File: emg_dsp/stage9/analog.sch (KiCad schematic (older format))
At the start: 27 parts, among them U35 OMNETICS_36, U36 MIC5365-2.7, U37 TC1016-3.0, U39 9X100, U40 ADCS7476, U41 9X100, U45 RHA2132

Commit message: boards done!! now need to produce gerbers etc.
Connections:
- wire segments 117 -> 113
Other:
- moved on the sheet: R47, R48, R52, R54

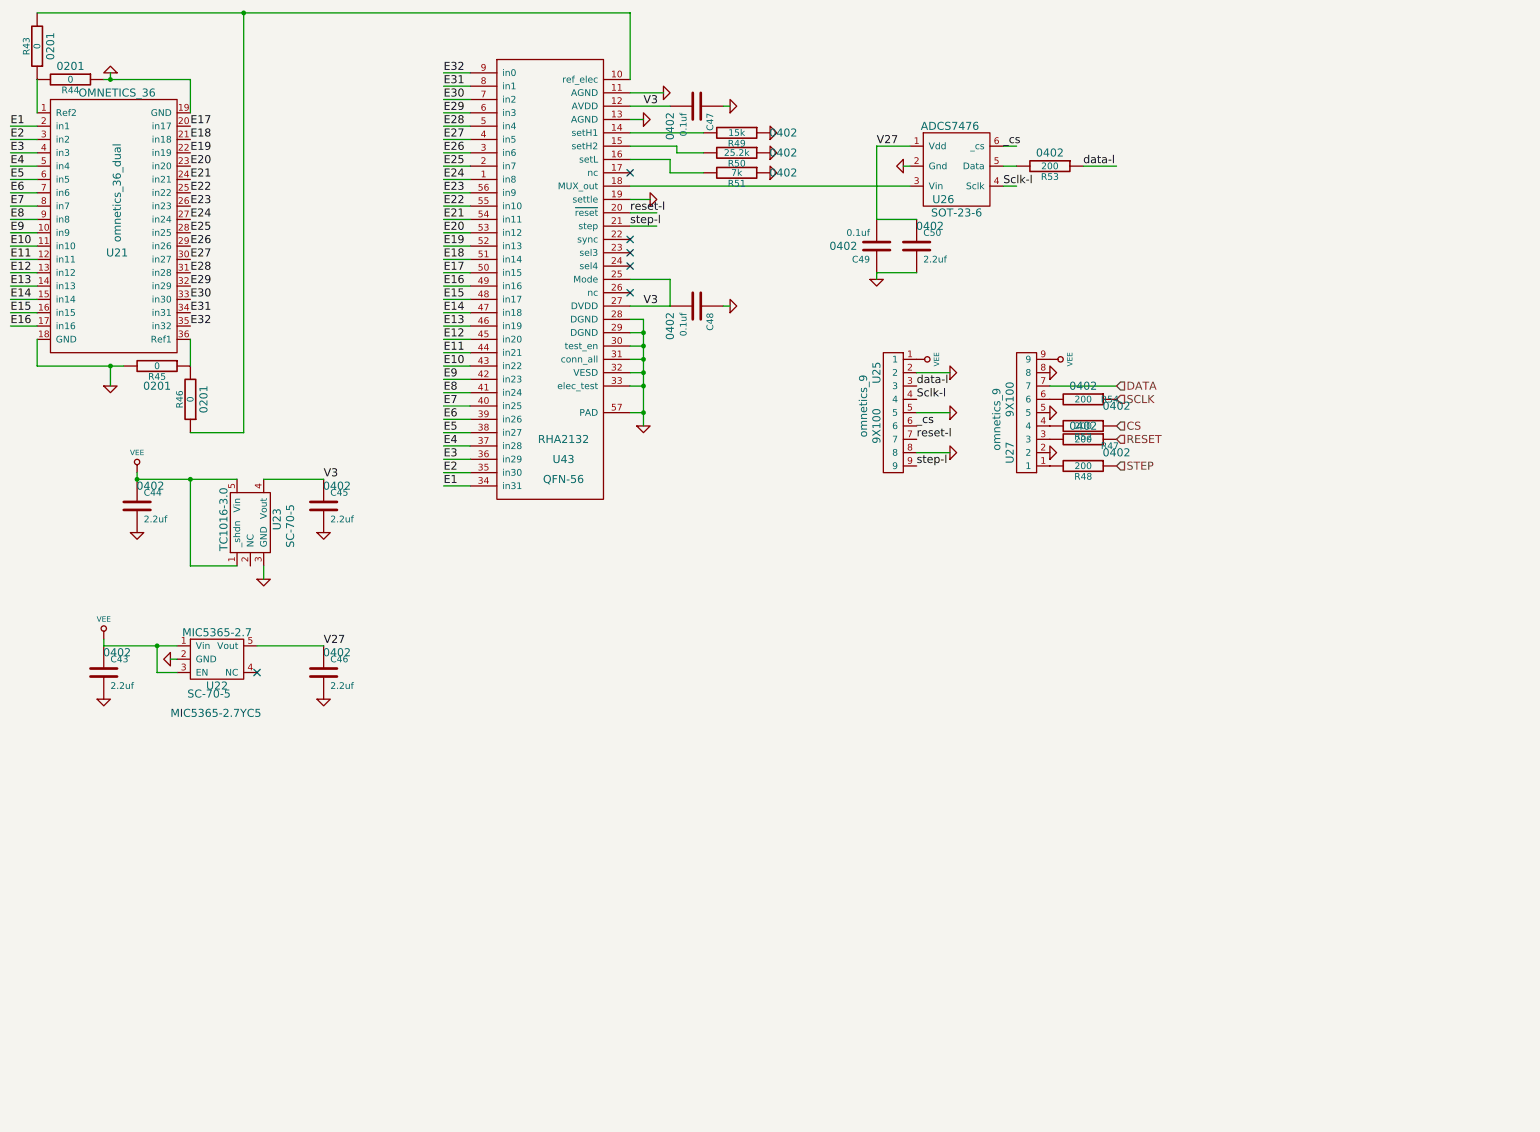
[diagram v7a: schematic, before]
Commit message: cleaned up firingrate.h -- not sure why this was not commited!
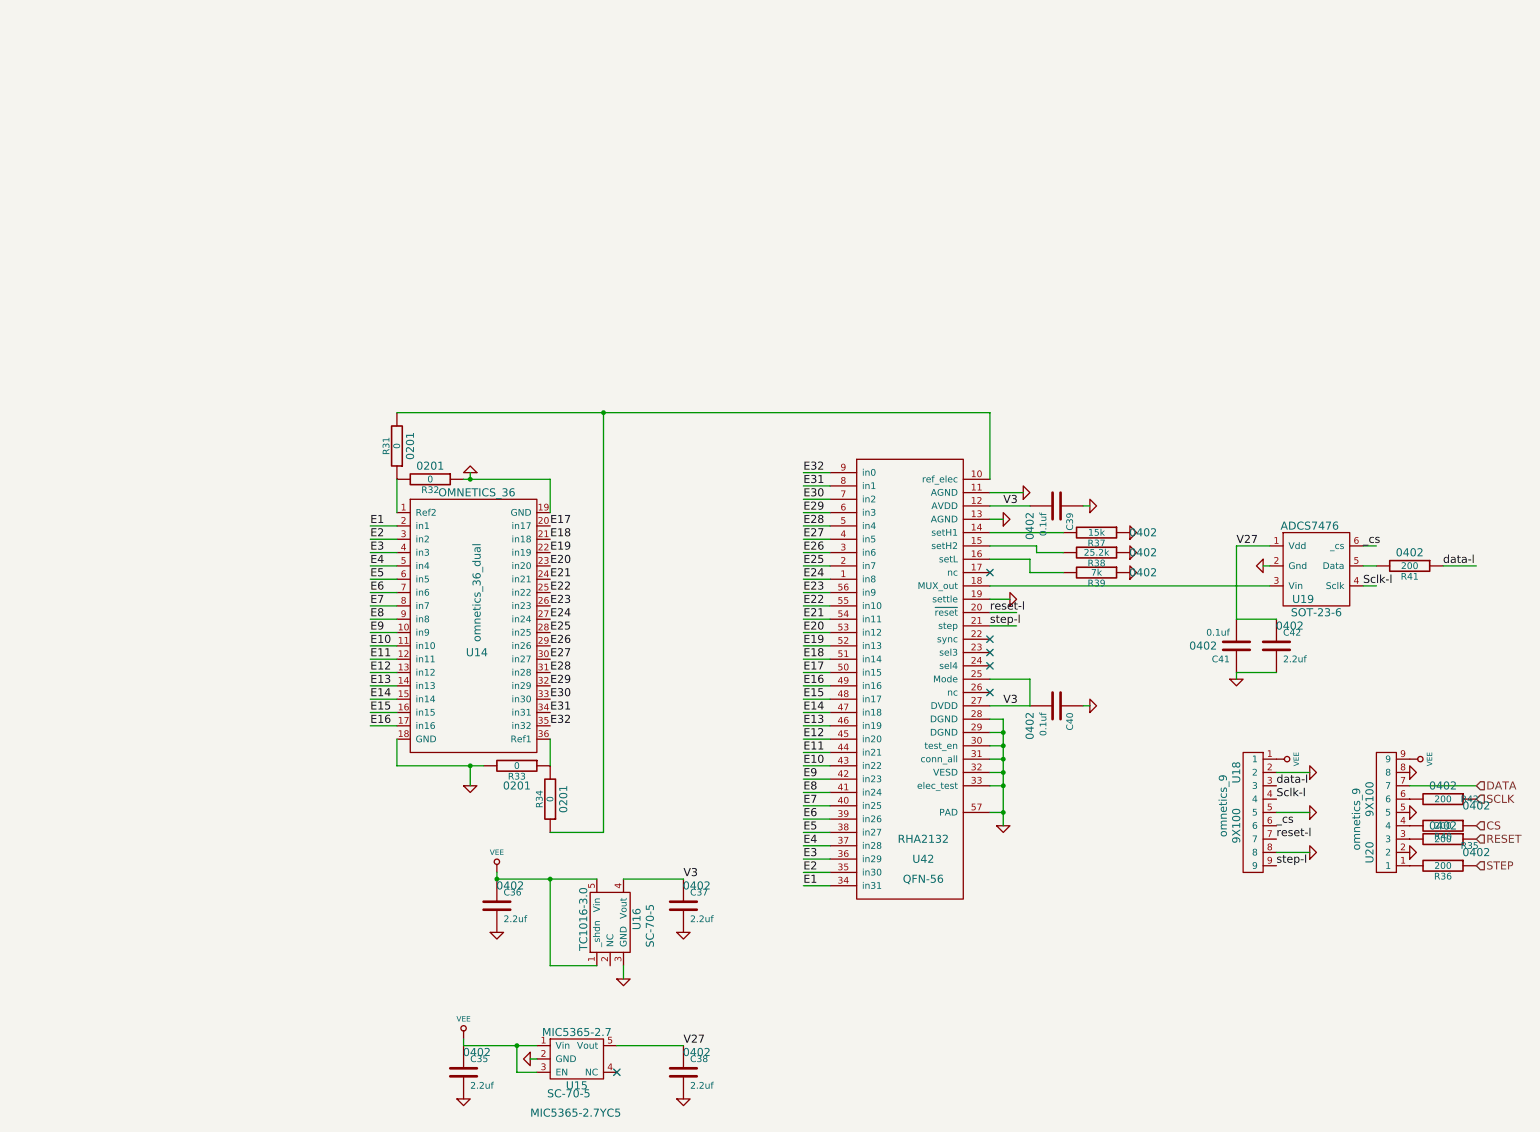
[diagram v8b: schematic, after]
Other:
- moved on the sheet: C35, C36, C37, C38, C39, C40, C41, C42, R31, R32, R33, R34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
